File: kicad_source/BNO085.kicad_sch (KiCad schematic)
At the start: 22 parts, among them U1 BNO085, Y1 DNI

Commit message: added page with outputs
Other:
- title: NavShieldBNO -> CyphalRobotController07/CAN
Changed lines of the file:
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@@
   (paper "A4")
   (title_block
-    (title "NavShieldBNO")
-    (date "2020-09-27")
+    (title "CyphalRobotController07/CAN")
+    (date "2023-10-01")
     (rev "0.1")
     (company "generationmake")

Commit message: started layout
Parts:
- removed R1, R2, R5, R7: 10k, resistors:R_0603, symbol NavShieldBNO-rescue:R_0603-devices
- removed W1, W2: TEST_1P, wire_pads:SolderWirePad_single_1mmSMD, symbol NavShieldBNO-rescue:TEST_1P-mechanical-connectors
- R51: renamed from R6; value DNI -> 0R
- R52: renamed from R8; value DNI -> 0R
- renumbered C1 to C48, C2 to C49, C3 to C50, C6 to C51, C7 to C52, R3 to R48, R4 to R49, R26 to R50, R9 to R53, R10 to R54, R11 to R55, R12 to R56, U1 to U16, Y1 to Y2
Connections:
- net ENV_SCL: no longer names the net of U16.15 (ENV_SCL)
- net ENV_SDA: no longer names the net of U16.16 (ENV_SDA)
- no-connect marks 0 -> 2

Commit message: made first draft of placement
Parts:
- C48, C49, C50, C51, C52: footprint capacitors:C_0603 -> Capacitor_SMD:C_0603_1608Metric
- R48, R49, R50, R51, R52, R53, R54, R55, R56: footprint resistors:R_0603 -> Resistor_SMD:R_0603_1608Metric
- U16: footprint LGA:LGA-28-5832 -> Package_LGA:LGA-28_5.2x3.8mm_P0.5mm
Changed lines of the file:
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@@
       (effects (font (size 1.524 1.524)))
     )
-    (property "Footprint" "LGA:LGA-28-5832" (id 2) (at 78.74 82.55 0)
+    (property "Footprint" "Package_LGA:LGA-28_5.2x3.8mm_P0.5mm" (id 2) (at 78.74 82.55 0)
       (effects (font (size 1.524 1.524)) hide)
     )
@@
       (effects (font (size 1.27 1.27)) (justify left))
     )
-    (property "Footprint" "resistors:R_0603" (id 2) (at 134.62 44.45 0)
+    (property "Footprint" "Resistor_SMD:R_0603_1608Metric" (id 2) (at 134.62 44.45 0)
       (effects (font (size 1.27 1.27)) hide)
     )
@@
       (effects (font (size 1.27 1.27)) (justify left))
     )
-    (property "Footprint" "resistors:R_0603" (id 2) (at 143.51 44.45 0)
+    (property "Footprint" "Resistor_SMD:R_0603_1608Metric" (id 2) (at 143.51 44.45 0)
       (effects (font (size 1.27 1.27)) hide)
     )
@@
       (effects (font (size 1.27 1.27)) (justify left))
     )
-    (property "Footprint" "capacitors:C_0603" (id 2) (at 35.56 67.31 0)
+    (property "Footprint" "Capacitor_SMD:C_0603_1608Metric" (id 2) (at 35.56 67.31 0)
       (effects (font (size 1.27 1.27)) hide)
     )
@@
       (effects (font (size 1.27 1.27)) (justify left))
     )
-    (property "Footprint" "resistors:R_0603" (id 2) (at 154.94 102.87 0)
+    (property "Footprint" "Resistor_SMD:R_0603_1608Metric" (id 2) (at 154.94 102.87 0)
       (effects (font (size 1.27 1.27)) hide)
     )
@@
       (effects (font (size 1.27 1.27)) (justify left))
     )
-    (property "Footprint" "resistors:R_0603" (id 2) (at 154.94 95.25 0)
+    (property "Footprint" "Resistor_SMD:R_0603_1608Metric" (id 2) (at 154.94 95.25 0)
       (effects (font (size 1.27 1.27)) hide)
     )
@@
     (property "Reference" "R56" (id 0) (at 160.02 60.96 90))
     (property "Value" "DNI" (id 1) (at 151.13 63.5 90))
-    (property "Footprint" "resistors:R_0603" (id 2) (at 160.02 62.23 0)
+    (property "Footprint" "Resistor_SMD:R_0603_1608Metric" (id 2) (at 160.02 62.23 0)
       (effects (font (size 1.27 1.27)) hide)
     )
@@
     (property "Reference" "R55" (id 0) (at 160.02 58.42 90))
     (property "Value" "DNI" (id 1) (at 151.13 60.96 90))
-    (property "Footprint" "resistors:R_0603" (id 2) (at 160.02 59.69 0)
+    (property "Footprint" "Resistor_SMD:R_0603_1608Metric" (id 2) (at 160.02 59.69 0)
       (effects (font (size 1.27 1.27)) hide)
     )
@@
       (effects (font (size 1.27 1.27)) (justify left))
     )
-    (property "Footprint" "resistors:R_0603" (id 2) (at 124.46 45.72 0)
+    (property "Footprint" "Resistor_SMD:R_0603_1608Metric" (id 2) (at 124.46 45.72 0)
       (effects (font (size 1.27 1.27)) hide)
     )
@@
       (effects (font (size 1.27 1.27)) (justify left))
     )
-    (property "Footprint" "resistors:R_0603" (id 2) (at 46.99 58.42 0)
+    (property "Footprint" "Resistor_SMD:R_0603_1608Metric" (id 2) (at 46.99 58.42 0)
       (effects (font (size 1.27 1.27)) hide)
     )
@@
       (effects (font (size 1.27 1.27)) (justify left))
     )
-    (property "Footprint" "capacitors:C_0603" (id 2) (at 22.86 31.75 0)
+    (property "Footprint" "Capacitor_SMD:C_0603_1608Metric" (id 2) (at 22.86 31.75 0)
       (effects (font (size 1.27 1.27)) hide)
     )
@@
       (effects (font (size 1.27 1.27)) (justify left))
     )
-    (property "Footprint" "capacitors:C_0603" (id 2) (at 35.56 31.75 0)
+    (property "Footprint" "Capacitor_SMD:C_0603_1608Metric" (id 2) (at 35.56 31.75 0)
       (effects (font (size 1.27 1.27)) hide)
     )
@@
       (effects (font (size 1.27 1.27)) (justify left))
     )
-    (property "Footprint" "resistors:R_0603" (id 2) (at 53.34 50.8 0)
+    (property "Footprint" "Resistor_SMD:R_0603_1608Metric" (id 2) (at 53.34 50.8 0)
       (effects (font (size 1.27 1.27)) hide)
     )
@@
       (effects (font (size 1.27 1.27)) (justify left))
     )
-    (property "Footprint" "capacitors:C_0603" (id 2) (at 124.46 38.1 0)
+    (property "Footprint" "Capacitor_SMD:C_0603_1608Metric" (id 2) (at 124.46 38.1 0)
       (effects (font (size 1.27 1.27)) hide)
     )
@@
       (effects (font (size 1.27 1.27)) (justify left))
     )
-    (property "Footprint" "capacitors:C_0603" (id 2) (at 124.46 27.94 0)
-      (effects (font (size 1.27 1.27)) hide)
-    )
+    (property "Footprint" "Capacitor_SMD:C_0603_1608Metric" (id 2) (at 124.46 27.94 0)
+      (effects (font (size 1.27 1.27)) hide)
+    )

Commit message: updated layout
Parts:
- Y2: footprint crystals:Crystal_SMD_3.2x1.5mm_2Pad -> Crystal:Crystal_SMD_3215-2Pin_3.2x1.5mm
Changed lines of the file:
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@@
       (effects (font (size 1.27 1.27)) (justify left))
     )
-    (property "Footprint" "crystals:Crystal_SMD_3.2x1.5mm_2Pad" (id 2) (at 112.7252 35.3314 90)
+    (property "Footprint" "Crystal:Crystal_SMD_3215-2Pin_3.2x1.5mm" (id 2) (at 112.7252 35.3314 90)
       (effects (font (size 1.27 1.27)) (justify left) hide)
     )

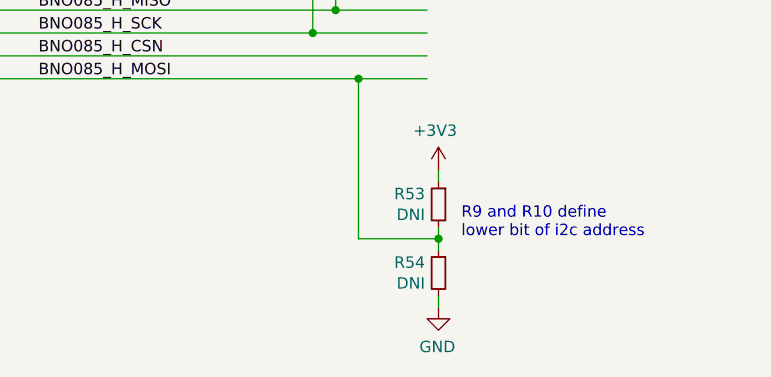
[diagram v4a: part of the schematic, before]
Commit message: updated schematic pdf
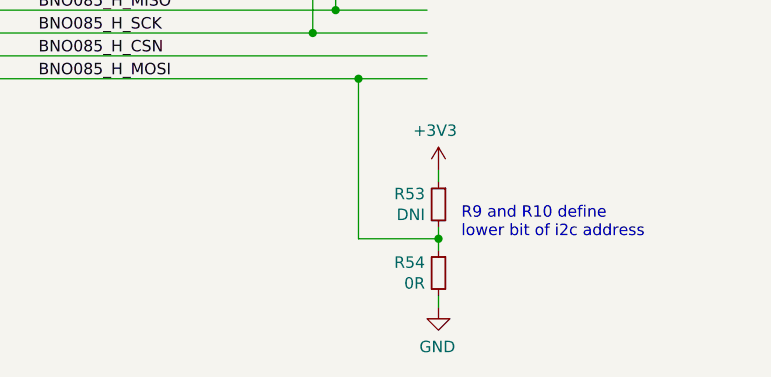
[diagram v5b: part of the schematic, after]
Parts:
- R54: value DNI -> 0R
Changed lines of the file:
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@@
   (title_block
     (title "CyphalRobotController07/CAN")
-    (date "2023-10-01")
+    (date "2023-10-02")
     (rev "0.1")
     (company "generationmake")
@@
       (effects (font (size 1.27 1.27)) (justify left))
     )
-    (property "Value" "DNI" (id 1) (at 153.4414 100.203 0)
-      (effects (font (size 1.27 1.27)) (justify left))
-    )
+    (property "Value" "0R" (id 1) (at 153.4414 100.203 0)
+      (effects (font (size 1.27 1.27)) (justify left))
+    )

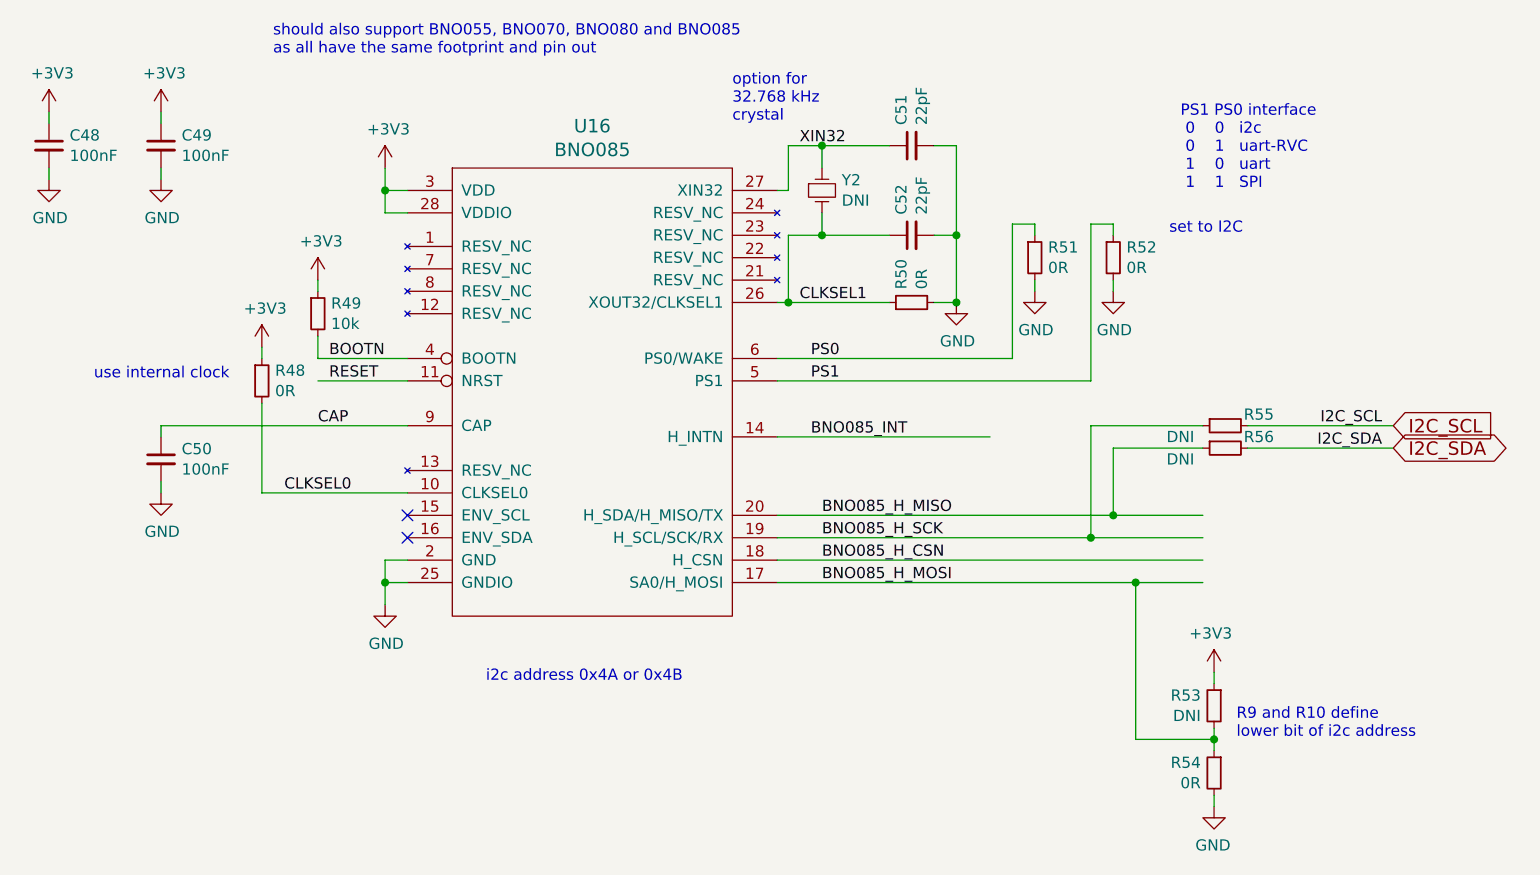
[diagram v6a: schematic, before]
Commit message: combined 3.3V nets
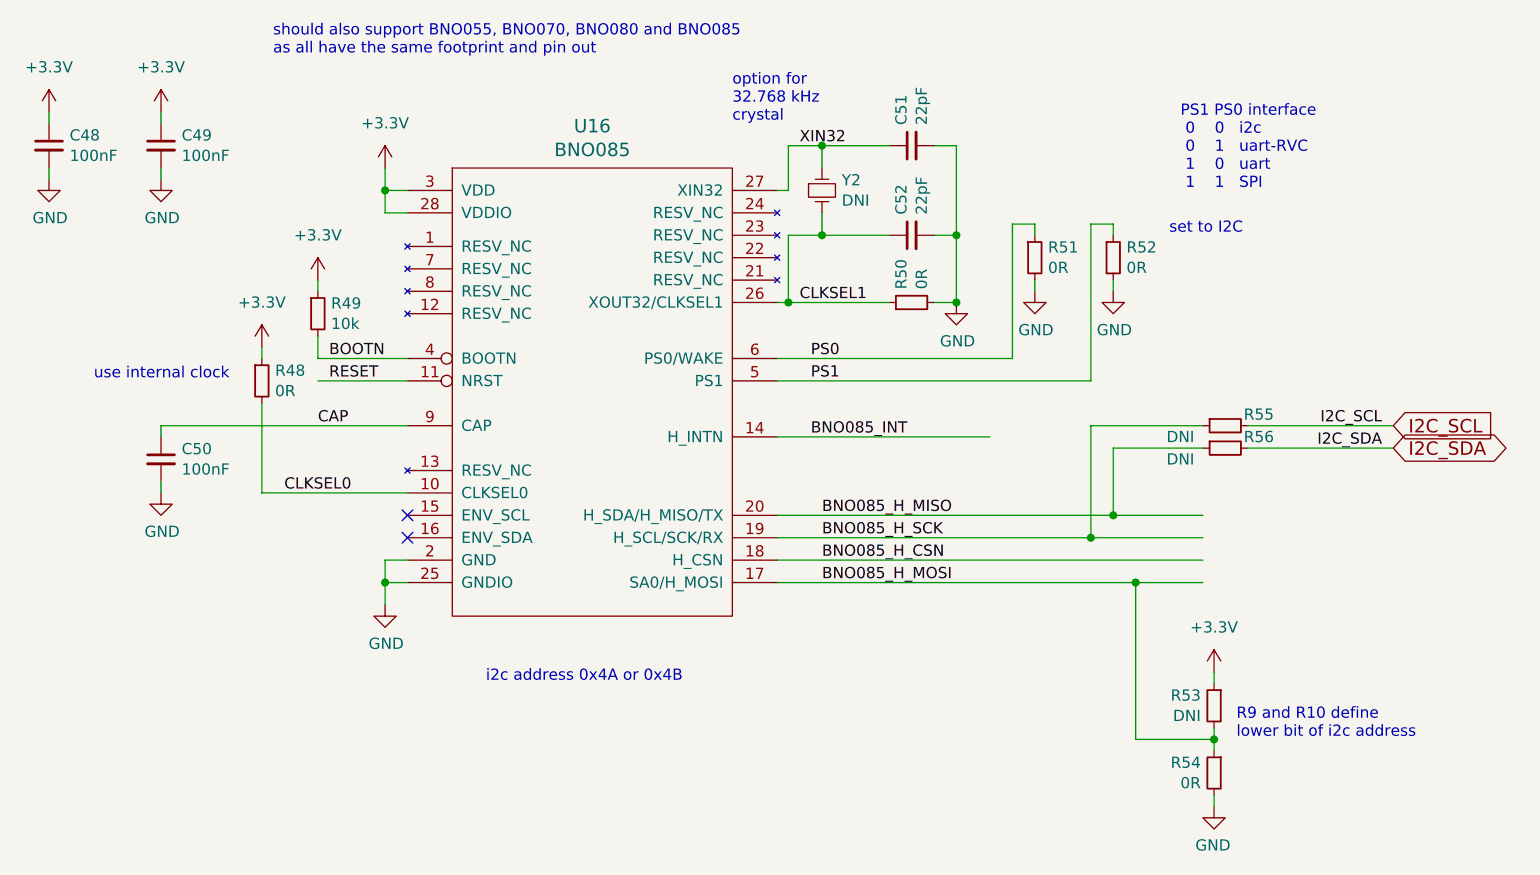
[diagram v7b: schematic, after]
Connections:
- net +3V3 renamed +3.3V
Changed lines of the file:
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@@
   (title_block
     (title "CyphalRobotController07/CAN")
-    (date "2023-11-15")
-    (rev "0.1")
+    (date "2023-12-03")
+    (rev "0.2")
     (company "generationmake")
   )
@@
     (pin "1")
   )
-  (symbol (lib_id "NavShieldBNO-rescue:+3V3-power-supply") (at 60.96 30.48 0) (unit 1)
-    (in_bom yes) (on_board yes)
-    (property "Reference" "#PWR0141" (id 0) (at 60.96 34.29 0)
-      (effects (font (size 1.27 1.27)) hide)
-    )
-    (property "Value" "+3V3" (id 1) (at 61.341 26.0858 0))
-    (property "Footprint" "" (id 2) (at 60.96 30.48 0))
-    (property "Datasheet" "" (id 3) (at 60.96 30.48 0))
-    (pin "1")
-  )
   (symbol (lib_id "NavShieldBNO-rescue:R_0603-devices") (at 134.62 40.64 0) (unit 1)
     (in_bom yes) (on_board yes)
@@
     (pin "2")
   )
-  (symbol (lib_id "NavShieldBNO-rescue:+3V3-power-supply") (at 154.94 87.63 0) (mirror y) (unit 1)
-    (in_bom yes) (on_board yes)
-    (property "Reference" "#PWR0146" (id 0) (at 154.94 91.44 0)
-      (effects (font (size 1.27 1.27)) hide)
-    )
-    (property "Value" "+3V3" (id 1) (at 154.559 83.2358 0))
-    (property "Footprint" "" (id 2) (at 154.94 87.63 0))
-    (property "Datasheet" "" (id 3) (at 154.94 87.63 0))
-    (pin "1")
-  )
   (symbol (lib_id "NavShieldBNO-rescue:GND-power-supply") (at 154.94 102.87 0) (mirror y) (unit 1)
     (in_bom yes) (on_board yes)
@@
     (pin "2")
   )
-  (symbol (lib_id "NavShieldBNO-rescue:+3V3-power-supply") (at 46.99 50.8 0) (unit 1)
-    (in_bom yes) (on_board yes)
-    (property "Reference" "#PWR0139" (id 0) (at 46.99 54.61 0)
-      (effects (font (size 1.27 1.27)) hide)
-    )
-    (property "Value" "+3V3" (id 1) (at 47.371 46.4058 0))
-    (property "Footprint" "" (id 2) (at 46.99 50.8 0))
-    (property "Datasheet" "" (id 3) (at 46.99 50.8 0))
-    (pin "1")
-  )
   (symbol (lib_id "NavShieldBNO-rescue:C_0603-devices") (at 22.86 27.94 0) (unit 1)
     (in_bom yes) (on_board yes)
@@
     (pin "1")
   )
-  (symbol (lib_id "NavShieldBNO-rescue:+3V3-power-supply") (at 22.86 24.13 0) (unit 1)
-    (in_bom yes) (on_board yes)
-    (property "Reference" "#PWR0134" (id 0) (at 22.86 27.94 0)
-      (effects (font (size 1.27 1.27)) hide)
-    )
-    (property "Value" "+3V3" (id 1) (at 23.241 19.7358 0))
-    (property "Footprint" "" (id 2) (at 22.86 24.13 0))
-    (property "Datasheet" "" (id 3) (at 22.86 24.13 0))
-    (pin "1")
-  )
   (symbol (lib_id "NavShieldBNO-rescue:C_0603-devices") (at 35.56 27.94 0) (unit 1)
     (in_bom yes) (on_board yes)
@@
     (pin "1")
   )
-  (symbol (lib_id "NavShieldBNO-rescue:+3V3-power-supply") (at 35.56 24.13 0) (unit 1)
-    (in_bom yes) (on_board yes)
-    (property "Reference" "#PWR0136" (id 0) (at 35.56 27.94 0)
-      (effects (font (size 1.27 1.27)) hide)
-    )
-    (property "Value" "+3V3" (id 1) (at 35.941 19.7358 0))
-    (property "Footprint" "" (id 2) (at 35.56 24.13 0))
-    (property "Datasheet" "" (id 3) (at 35.56 24.13 0))
-    (pin "1")
-  )
   (symbol (lib_id "NavShieldBNO-rescue:R_0603-devices") (at 53.34 46.99 0) (unit 1)
     (in_bom yes) (on_board yes)
@@
     (pin "1")
     (pin "2")
-  )
-  (symbol (lib_id "NavShieldBNO-rescue:+3V3-power-supply") (at 53.34 43.18 0) (unit 1)
-    (in_bom yes) (on_board yes)
-    (property "Reference" "#PWR0140" (id 0) (at 53.34 46.99 0)
-      (effects (font (size 1.27 1.27)) hide)
-    )
-    (property "Value" "+3V3" (id 1) (at 53.721 38.7858 0))
-    (property "Footprint" "" (id 2) (at 53.34 43.18 0))
-    (property "Datasheet" "" (id 3) (at 53.34 43.18 0))
-    (pin "1")
   )
   (symbol (lib_id "NavShieldBNO-rescue:Crystal_Small-devices") (at 110.49 33.02 270) (unit 1)
@@
     (pin "2")
   )
+  (symbol (lib_id "power:+3.3V") (at 22.86 24.13 0) (unit 1)
+    (in_bom yes) (on_board yes) (fields_autoplaced)
+    (property "Reference" "#PWR0156" (id 0) (at 22.86 27.94 0)
+      (effects (font (size 1.27 1.27)) hide)
+    )
+    (property "Value" "+3.3V" (id 1) (at 22.86 19.05 0))
+    (property "Footprint" "" (id 2) (at 22.86 24.13 0)
+      (effects (font (size 1.27 1.27)) hide)
+    )
+    (property "Datasheet" "" (id 3) (at 22.86 24.13 0)
+      (effects (font (size 1.27 1.27)) hide)
+    )
+    (pin "1")
+  )
+  (symbol (lib_id "power:+3.3V") (at 60.96 30.48 0) (unit 1)
+    (in_bom yes) (on_board yes) (fields_autoplaced)
+    (property "Reference" "#PWR0159" (id 0) (at 60.96 34.29 0)
+      (effects (font (size 1.27 1.27)) hide)
+    )
+    (property "Value" "+3.3V" (id 1) (at 60.96 25.4 0))
+    (property "Footprint" "" (id 2) (at 60.96 30.48 0)
+      (effects (font (size 1.27 1.27)) hide)
+    )
+    (property "Datasheet" "" (id 3) (at 60.96 30.48 0)
+      (effects (font (size 1.27 1.27)) hide)
+    )
+    (pin "1")
+  )
+  (symbol (lib_id "power:+3.3V") (at 35.56 24.13 0) (unit 1)
+    (in_bom yes) (on_board yes) (fields_autoplaced)
+    (property "Reference" "#PWR0157" (id 0) (at 35.56 27.94 0)
+      (effects (font (size 1.27 1.27)) hide)
+    )
+    (property "Value" "+3.3V" (id 1) (at 35.56 19.05 0))
+    (property "Footprint" "" (id 2) (at 35.56 24.13 0)
+      (effects (font (size 1.27 1.27)) hide)
+    )
+    (property "Datasheet" "" (id 3) (at 35.56 24.13 0)
+      (effects (font (size 1.27 1.27)) hide)
+    )
+    (pin "1")
+  )
+  (symbol (lib_id "power:+3.3V") (at 154.94 87.63 0) (unit 1)
+    (in_bom yes) (on_board yes) (fields_autoplaced)
+    (property "Reference" "#PWR0158" (id 0) (at 154.94 91.44 0)
+      (effects (font (size 1.27 1.27)) hide)
+    )
+    (property "Value" "+3.3V" (id 1) (at 154.94 82.55 0))
+    (property "Footprint" "" (id 2) (at 154.94 87.63 0)
+      (effects (font (size 1.27 1.27)) hide)
+    )
+    (property "Datasheet" "" (id 3) (at 154.94 87.63 0)
+      (effects (font (size 1.27 1.27)) hide)
+    )
+    (pin "1")
+  )
+  (symbol (lib_id "power:+3.3V") (at 46.99 50.8 0) (unit 1)
+    (in_bom yes) (on_board yes) (fields_autoplaced)
+    (property "Reference" "#PWR0155" (id 0) (at 46.99 54.61 0)
+      (effects (font (size 1.27 1.27)) hide)
+    )
+    (property "Value" "+3.3V" (id 1) (at 46.99 45.72 0))
+    (property "Footprint" "" (id 2) (at 46.99 50.8 0)
+      (effects (font (size 1.27 1.27)) hide)
+    )
+    (property "Datasheet" "" (id 3) (at 46.99 50.8 0)
+      (effects (font (size 1.27 1.27)) hide)
+    )
+    (pin "1")
+  )
+  (symbol (lib_id "power:+3.3V") (at 53.34 43.18 0) (unit 1)
+    (in_bom yes) (on_board yes) (fields_autoplaced)
+    (property "Reference" "#PWR0154" (id 0) (at 53.34 46.99 0)
+      (effects (font (size 1.27 1.27)) hide)
+    )
+    (property "Value" "+3.3V" (id 1) (at 53.34 38.1 0))
+    (property "Footprint" "" (id 2) (at 53.34 43.18 0)
+      (effects (font (size 1.27 1.27)) hide)
+    )
+    (property "Datasheet" "" (id 3) (at 53.34 43.18 0)
+      (effects (font (size 1.27 1.27)) hide)
+    )
+    (pin "1")
+  )
   (sheet_instances
